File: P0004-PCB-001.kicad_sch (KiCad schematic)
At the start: 24 parts, among them CN1 Molex 105057-0001, CN2 104031-0811, CN3 Liansheng PH--00603, SW1 Khon TSB06331-090D332DA-R0500, SW2 Khon TSB06331-090D332DA-R0500, SW3 Khon TSB06331-090D332DA-R0500, SW4 Khon TSB06331-090D332DA-R0500

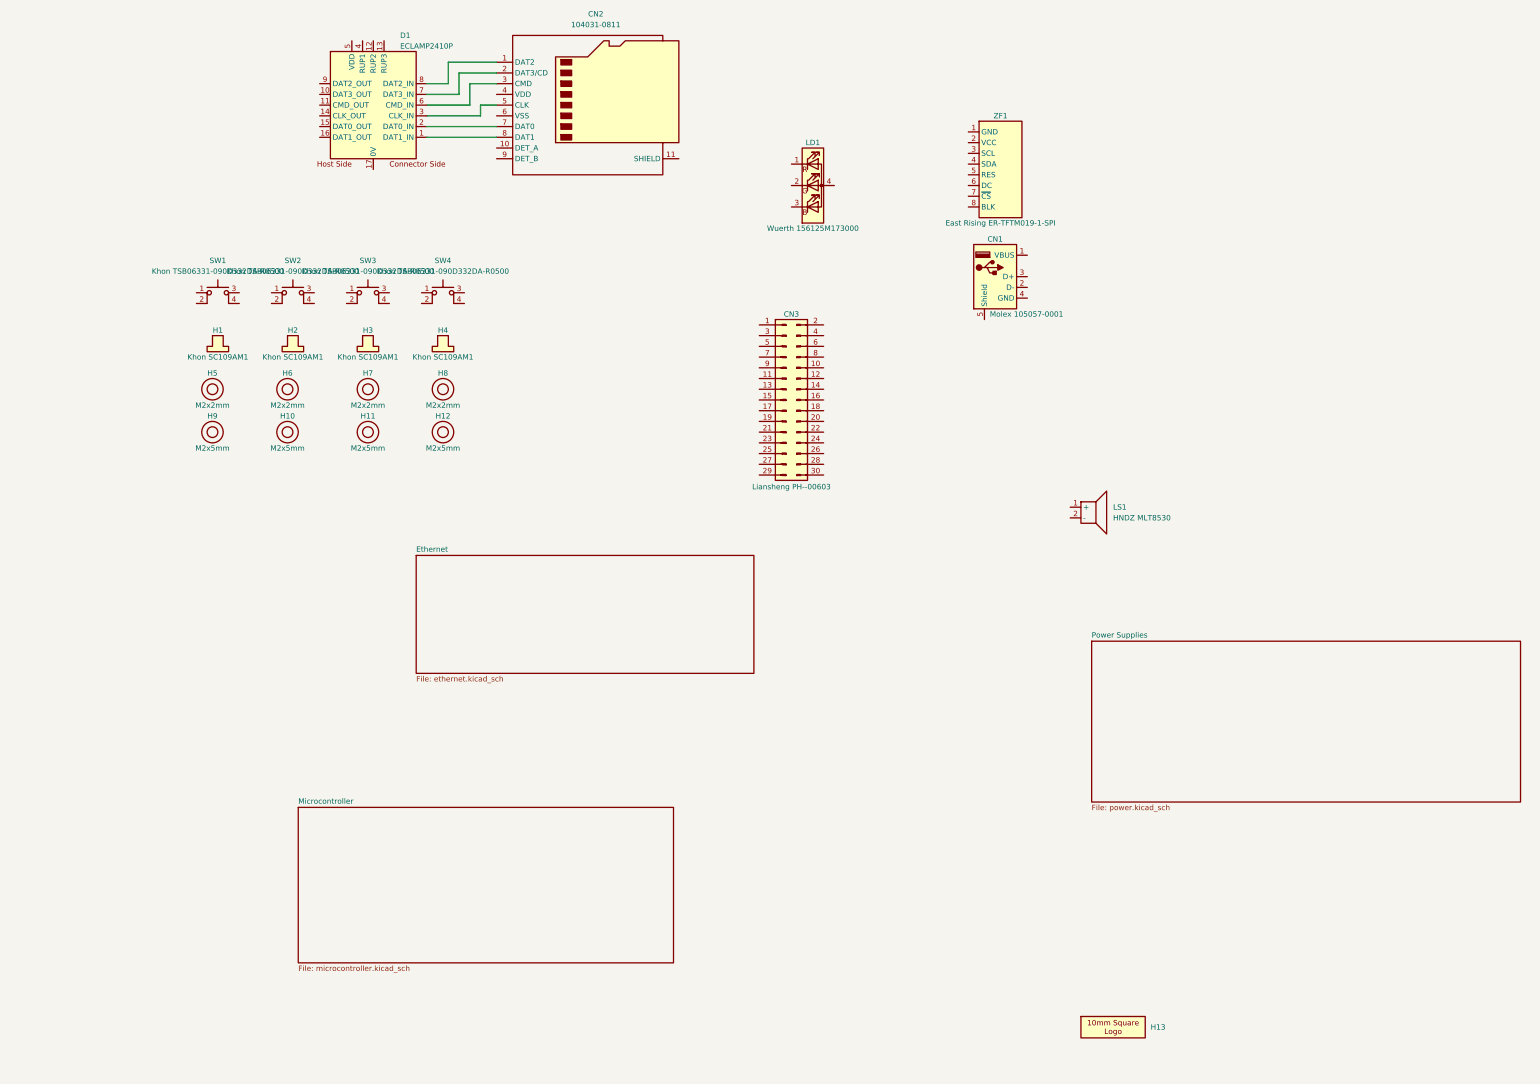
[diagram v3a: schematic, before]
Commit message: added ethernet phy
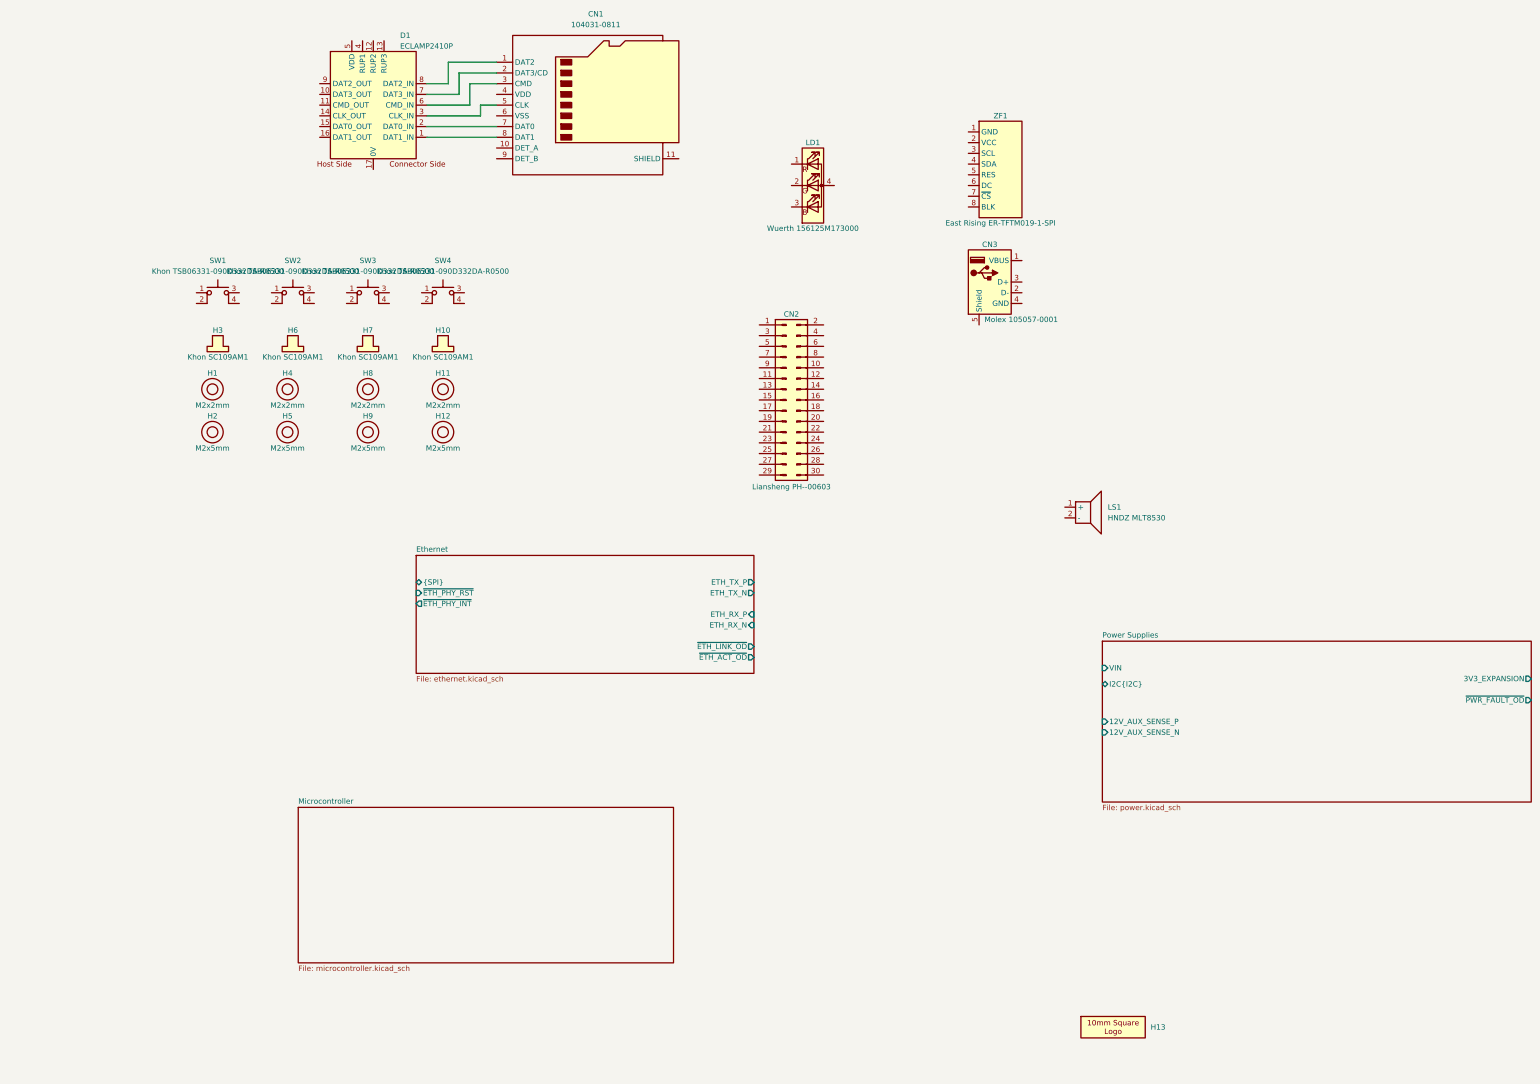
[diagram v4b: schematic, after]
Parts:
- renumbered CN2 to CN1, CN3 to CN2, CN1 to CN3, H5 to H1, H4 to H10, H8 to H11, H9 to H2, H1 to H3, H6 to H4, H10 to H5, H2 to H6, H3 to H7, H7 to H8, H11 to H9
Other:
- sheet Ethernet ports: added ETH_RX_N, ETH_RX_P, ETH_TX_N, ETH_TX_P, {SPI}, ~{ETH_ACT_OD}, ~{ETH_LINK_OD}, ~{ETH_PHY_INT}, ~{ETH_PHY_RST}; removed none
- sheet Power Supplies ports: added 12V_AUX_SENSE_N, 12V_AUX_SENSE_P, 3V3_EXPANSION, I2C{I2C}, VIN, ~{PWR_FAULT_OD}; removed none
- moved on the sheet: CN3, LS1

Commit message: layout progress
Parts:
- added D12: USBLC6-2P6, Package_TO_SOT_SMD:SOT-666, symbol Diode_WUT:ST_USBLC6-2P6
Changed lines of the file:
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@@
+	)
+	(symbol
+		(lib_id "Diode_WUT:ST_USBLC6-2P6")
+		(at 248.92 119.38 0)
+		(unit 1)
+		(body_style 1)
+		(exclude_from_sim no)
+		(in_bom yes)
+		(on_board yes)
+		(in_pos_files yes)
+		(dnp no)
+		(fields_autoplaced yes)
+		(property "Reference" "D12"
+			(at 250.19 115.57 0)
+			(show_name no)
+			(do_not_autoplace yes)
+			(effects
+				(font
+					(size 1.27 1.27)
+				)
+				(justify left)
+			)
+		)
+		(property "Value" "USBLC6-2P6"
+			(at 250.19 126.365 0)
+			(show_name no)
+			(do_not_autoplace yes)
+			(effects
+				(font
+					(size 1.27 1.27)
+				)
+				(justify left)
+			)
+		)
+		(property "Footprint" "Package_TO_SOT_SMD:SOT-666"
+			(at 248.92 119.38 0)
+			(hide yes)
+			(show_name no)
+			(do_not_autoplace no)
+			(effects
+				(font
+					(size 1.27 1.27)
+				)
+			)
+		)
+		(property "Datasheet" "https://www.st.com/content/ccc/resource/technical/document/datasheet/06/1d/48/9c/6c/20/4a/b2/CD00050750.pdf/files/CD00050750.pdf/jcr:content/translations/en.CD00050750.pdf"
+			(at 248.92 119.38 0)
+			(hide yes)
+			(show_name no)
+			(do_not_autoplace no)
+			(effects
+				(font
+					(size 1.27 1.27)
+				)
+			)
+		)
+		(property "Description" ""
+			(at 248.92 119.38 0)
+			(hide yes)
+			(show_name no)
+			(do_not_autoplace no)
+			(effects
+				(font
+					(size 1.27 1.27)
+				)
+			)
+		)
+		(property "Manufacturer" "ST"
+			(at 248.92 119.38 0)
+			(hide yes)
+			(show_name no)
+			(do_not_autoplace no)
+			(effects
+				(font
+					(size 1.27 1.27)
+				)
+			)
+		)
+		(property "MPN" "USBLC6-2P6"
+			(at 248.92 119.38 0)
+			(hide yes)
+			(show_name no)
+			(do_not_autoplace no)
+			(effects
+				(font
+					(size 1.27 1.27)
+				)
+			)
+		)
+		(pin "6"
+		)
+		(pin "4"
+		)
+		(pin "3"
+		)
+		(pin "2"
+		)
+		(pin "5"
+		)
+		(pin "1"
+		)
+		(instances
+			(project "P0004-PCB-001"
+				(path "/acdb93e6-9aa6-4a78-8a68-9d0ae3318f45"
+					(reference "D12")
+					(unit 1)
+				)
+			)
+		)
 	)
 	(symbol

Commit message: wup
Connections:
- net at D12.1 (I/O1): now also CN3.3 (D+)
- net at D12.3 (I/O2): now also CN3.2 (D-)
- net 5V_VBUS: now reaches CN3.1 (VBUS)
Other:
- moved on the sheet: D12
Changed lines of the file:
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@@
+	(wire
+		(pts
+			(xy 251.46 93.98) (xy 259.08 93.98)
+		)
+		(stroke
+			(width 0)
+			(type default)
+		)
+	)
+	(wire
+		(pts
+			(xy 251.46 96.52) (xy 259.08 96.52)
+		)
+		(stroke
+			(width 0)
+			(type default)
+		)
+	)
 	(wire
 		(pts
@@
 	(wire
 		(pts
-			(xy 110.49 54.61) (xy 123.19 54.61)
+			(xy 256.54 86.36) (xy 256.54 88.9)
 		)
 		(stroke
@@
 	(wire
 		(pts
-			(xy 115.57 46.99) (xy 110.49 46.99)
+			(xy 110.49 54.61) (xy 123.19 54.61)
 		)
 		(stroke
@@
 	(wire
 		(pts
-			(xy 115.57 41.91) (xy 115.57 46.99)
+			(xy 115.57 46.99) (xy 110.49 46.99)
 		)
 		(stroke
@@
 	(wire
 		(pts
-			(xy 123.19 52.07) (xy 127 52.07)
+			(xy 115.57 41.91) (xy 115.57 46.99)
 		)
 		(stroke
@@
 	(wire
 		(pts
-			(xy 120.65 52.07) (xy 120.65 46.99)
+			(xy 123.19 52.07) (xy 127 52.07)
 		)
 		(stroke
@@
 	(wire
 		(pts
-			(xy 110.49 59.69) (xy 127 59.69)
+			(xy 120.65 52.07) (xy 120.65 46.99)
 		)
 		(stroke
@@
 	(wire
 		(pts
-			(xy 110.49 49.53) (xy 118.11 49.53)
+			(xy 110.49 59.69) (xy 127 59.69)
 		)
 		(stroke
@@
 	(wire
 		(pts
-			(xy 118.11 44.45) (xy 127 44.45)
+			(xy 110.49 49.53) (xy 118.11 49.53)
 		)
 		(stroke
@@
 	(wire
 		(pts
-			(xy 110.49 57.15) (xy 127 57.15)
+			(xy 118.11 44.45) (xy 127 44.45)
 		)
 		(stroke
@@
 	(wire
 		(pts
-			(xy 120.65 46.99) (xy 127 46.99)
+			(xy 110.49 57.15) (xy 127 57.15)
 		)
 		(stroke
@@
 	(wire
 		(pts
-			(xy 118.11 49.53) (xy 118.11 44.45)
+			(xy 120.65 46.99) (xy 127 46.99)
 		)
 		(stroke
@@
 	(wire
 		(pts
-			(xy 110.49 52.07) (xy 120.65 52.07)
+			(xy 118.11 49.53) (xy 118.11 44.45)
 		)
 		(stroke
@@
 	(wire
 		(pts
+			(xy 110.49 52.07) (xy 120.65 52.07)
+		)
+		(stroke
+			(width 0)
+			(type default)
+		)
+	)
+	(wire
+		(pts
 			(xy 127 41.91) (xy 115.57 41.91)
+		)
+		(stroke
+			(width 0)
+			(type default)
+		)
+	)
+	(wire
+		(pts
+			(xy 256.54 88.9) (xy 251.46 88.9)
 		)
 		(stroke
@@
 	(symbol
 		(lib_id "Diode_WUT:ST_USBLC6-2P6")
-		(at 248.92 119.38 0)
+		(at 264.16 93.98 0)
 		(unit 1)
 		(body_style 1)
@@
 		(fields_autoplaced yes)
 		(property "Reference" "D12"
-			(at 250.19 115.57 0)
+			(at 265.43 90.17 0)
 			(show_name no)
 			(do_not_autoplace yes)
@@
 		)
 		(property "Value" "USBLC6-2P6"
-			(at 250.19 126.365 0)
+			(at 265.43 100.965 0)
 			(show_name no)
 			(do_not_autoplace yes)
@@
 		)
 		(property "Footprint" "Package_TO_SOT_SMD:SOT-666"
-			(at 248.92 119.38 0)
+			(at 264.16 93.98 0)
 			(hide yes)
 			(show_name no)
@@
 		)
 		(property "Datasheet" "https://www.st.com/content/ccc/resource/technical/document/datasheet/06/1d/48/9c/6c/20/4a/b2/CD00050750.pdf/files/CD00050750.pdf/jcr:content/translations/en.CD00050750.pdf"
-			(at 248.92 119.38 0)
+			(at 264.16 93.98 0)
 			(hide yes)
 			(show_name no)
@@
 		)
 		(property "Description" ""
-			(at 248.92 119.38 0)
+			(at 264.16 93.98 0)
 			(hide yes)
 			(show_name no)
@@
 		)
 		(property "Manufacturer" "ST"
-			(at 248.92 119.38 0)
+			(at 264.16 93.98 0)
 			(hide yes)
 			(show_name no)
@@
 		)
 		(property "MPN" "USBLC6-2P6"
-			(at 248.92 119.38 0)
+			(at 264.16 93.98 0)
 			(hide yes)
 			(show_name no)
@@
 					(unit 1)
 				)
+			)
+		)
+	)
+	(symbol
+		(lib_id "Power_WUT:3V3")
+		(at 256.54 86.36 0)
+		(unit 1)
+		(body_style 1)
+		(exclude_from_sim no)
+		(in_bom no)
+		(on_board no)
+		(in_pos_files yes)
+		(dnp no)
+		(fields_autoplaced yes)
+		(property "Reference" "#PWR028"
+			(at 255.905 89.535 0)
+			(hide yes)
+			(show_name no)
+			(do_not_autoplace no)
+			(effects
+				(font
+					(size 1.27 1.27)
+				)
+			)
+		)
+		(property "Value" "5V_VBUS"
+			(at 256.54 82.55 0)
+			(show_name no)
+			(do_not_autoplace yes)
+			(effects
+				(font
+					(size 1.27 1.27)
+				)
+			)
+		)
+		(property "Footprint" ""
+			(at 256.54 86.36 0)
+			(hide yes)
+			(show_name no)
+			(do_not_autoplace no)
+			(effects
+				(font
+					(size 1.27 1.27)
+				)
+			)
+		)
+		(property "Datasheet" ""
+			(at 256.54 86.36 0)
+			(hide yes)
+			(show_name no)
+			(do_not_autoplace no)
+			(effects
+				(font
+					(size 1.27 1.27)
+				)
+			)
+		)
+		(property "Description" ""
+			(at 256.54 86.36 0)
+			(hide yes)
+			(show_name no)
+			(do_not_autoplace no)
+			(effects
+				(font
+					(size 1.27 1.27)
+				)
+			)
+		)
+		(pin "1"
+		)
+		(instances
+			(project "P0004-PCB-001"
+				(path "/acdb93e6-9aa6-4a78-8a68-9d0ae3318f45"
+					(reference "#PWR028")
+					(unit 1)
+				)

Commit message: did a few little bits on layout
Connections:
- net 5V_VBUS: now also D12.5 (VBUS)
- net 0V: now reaches D12.2 (GND)
- net 0V: now also CN3.4 (GND)
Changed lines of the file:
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@@
 	(generator_version "10.0")
 	(paper "A3")
+	(junction
+		(at 264.16 104.14)
+		(diameter 0)
+		(color 0 0 0 0)
+	)
+	(junction
+		(at 264.16 86.36)
+		(diameter 0)
+		(color 0 0 0 0)
+	)
+	(wire
+		(pts
+			(xy 251.46 88.9) (xy 256.54 88.9)
+		)
+		(stroke
+			(width 0)
+			(type default)
+		)
+	)
+	(wire
+		(pts
+			(xy 251.46 99.06) (xy 256.54 99.06)
+		)
+		(stroke
+			(width 0)
+			(type default)
+		)
+	)
 	(wire
 		(pts
@@
 	(wire
 		(pts
-			(xy 256.54 86.36) (xy 256.54 88.9)
+			(xy 264.16 104.14) (xy 264.16 106.68)
 		)
 		(stroke
@@
 	(wire
 		(pts
-			(xy 110.49 54.61) (xy 123.19 54.61)
+			(xy 264.16 83.82) (xy 264.16 86.36)
 		)
 		(stroke
@@
 	(wire
 		(pts
-			(xy 115.57 46.99) (xy 110.49 46.99)
+			(xy 110.49 54.61) (xy 123.19 54.61)
 		)
 		(stroke
@@
 	(wire
 		(pts
-			(xy 115.57 41.91) (xy 115.57 46.99)
+			(xy 115.57 46.99) (xy 110.49 46.99)
 		)
 		(stroke
@@
 	(wire
 		(pts
-			(xy 123.19 52.07) (xy 127 52.07)
+			(xy 115.57 41.91) (xy 115.57 46.99)
 		)
 		(stroke
@@
 	(wire
 		(pts
-			(xy 120.65 52.07) (xy 120.65 46.99)
+			(xy 123.19 52.07) (xy 127 52.07)
 		)
 		(stroke
@@
 	(wire
 		(pts
-			(xy 110.49 59.69) (xy 127 59.69)
+			(xy 256.54 86.36) (xy 264.16 86.36)
 		)
 		(stroke
@@
 	(wire
 		(pts
-			(xy 110.49 49.53) (xy 118.11 49.53)
+			(xy 256.54 104.14) (xy 264.16 104.14)
 		)
 		(stroke
@@
 	(wire
 		(pts
-			(xy 118.11 44.45) (xy 127 44.45)
+			(xy 120.65 52.07) (xy 120.65 46.99)
 		)
 		(stroke
@@
 	(wire
 		(pts
-			(xy 110.49 57.15) (xy 127 57.15)
+			(xy 264.16 86.36) (xy 264.16 88.9)
 		)
 		(stroke
@@
 	(wire
 		(pts
-			(xy 120.65 46.99) (xy 127 46.99)
+			(xy 110.49 59.69) (xy 127 59.69)
 		)
 		(stroke
@@
 	(wire
 		(pts
-			(xy 118.11 49.53) (xy 118.11 44.45)
+			(xy 110.49 49.53) (xy 118.11 49.53)
 		)
 		(stroke
@@
 	(wire
 		(pts
-			(xy 110.49 52.07) (xy 120.65 52.07)
+			(xy 118.11 44.45) (xy 127 44.45)
 		)
 		(stroke
@@
 	(wire
 		(pts
-			(xy 127 41.91) (xy 115.57 41.91)
+			(xy 256.54 99.06) (xy 256.54 104.14)
 		)
 		(stroke
@@
 	(wire
 		(pts
-			(xy 256.54 88.9) (xy 251.46 88.9)
+			(xy 110.49 57.15) (xy 127 57.15)
+		)
+		(stroke
+			(width 0)
+			(type default)
+		)
+	)
+	(wire
+		(pts
+			(xy 120.65 46.99) (xy 127 46.99)
+		)
+		(stroke
+			(width 0)
+			(type default)
+		)
+	)
+	(wire
+		(pts
+			(xy 256.54 88.9) (xy 256.54 86.36)
+		)
+		(stroke
+			(width 0)
+			(type default)
+		)
+	)
+	(wire
+		(pts
+			(xy 118.11 49.53) (xy 118.11 44.45)
+		)
+		(stroke
+			(width 0)
+			(type default)
+		)
+	)
+	(wire
+		(pts
+			(xy 110.49 52.07) (xy 120.65 52.07)
+		)
+		(stroke
+			(width 0)
+			(type default)
+		)
+	)
+	(wire
+		(pts
+			(xy 264.16 101.6) (xy 264.16 104.14)
+		)
+		(stroke
+			(width 0)
+			(type default)
+		)
+	)
+	(wire
+		(pts
+			(xy 127 41.91) (xy 115.57 41.91)
 		)
 		(stroke
@@
 	(symbol
 		(lib_id "Power_WUT:3V3")
-		(at 256.54 86.36 0)
+		(at 264.16 83.82 0)
 		(unit 1)
 		(body_style 1)
@@
 		(fields_autoplaced yes)
 		(property "Reference" "#PWR028"
-			(at 255.905 89.535 0)
+			(at 263.525 86.995 0)
 			(hide yes)
 			(show_name no)
@@
 		)
 		(property "Value" "5V_VBUS"
-			(at 256.54 82.55 0)
+			(at 264.16 80.01 0)
 			(show_name no)
 			(do_not_autoplace yes)
@@
 		)
 		(property "Footprint" ""
-			(at 256.54 86.36 0)
+			(at 264.16 83.82 0)
 			(hide yes)
 			(show_name no)
@@
 		)
 		(property "Datasheet" ""
-			(at 256.54 86.36 0)
+			(at 264.16 83.82 0)
 			(hide yes)
 			(show_name no)
@@
 		)
 		(property "Description" ""
-			(at 256.54 86.36 0)
+			(at 264.16 83.82 0)
 			(hide yes)
 			(show_name no)
@@
 					(unit 1)
 				)
+			)
+		)
+	)
+	(symbol
+		(lib_id "Power_WUT:0V")
+		(at 264.16 106.68 0)
+		(unit 1)
+		(body_style 1)
+		(exclude_from_sim no)
+		(in_bom no)
+		(on_board no)
+		(in_pos_files yes)
+		(dnp no)
+		(fields_autoplaced yes)
+		(property "Reference" "#PWR031"
+			(at 264.16 106.68 0)
+			(hide yes)
+			(show_name no)
+			(do_not_autoplace no)
+			(effects
+				(font
+					(size 1.27 1.27)
+				)
+			)
+		)
+		(property "Value" "0V"
+			(at 264.16 110.49 0)
+			(show_name no)
+			(do_not_autoplace yes)
+			(effects
+				(font
+					(size 1.27 1.27)
+				)
+			)
+		)
+		(property "Footprint" ""
+			(at 264.16 106.68 0)
+			(hide yes)
+			(show_name no)
+			(do_not_autoplace no)
+			(effects
+				(font
+					(size 1.27 1.27)
+				)
+			)
+		)
+		(property "Datasheet" ""
+			(at 264.16 106.68 0)
+			(hide yes)
+			(show_name no)
+			(do_not_autoplace no)
+			(effects
+				(font
+					(size 1.27 1.27)
+				)
+			)
+		)
+		(property "Description" ""
+			(at 264.16 106.68 0)
+			(hide yes)
+			(show_name no)
+			(do_not_autoplace no)
+			(effects
+				(font
+					(size 1.27 1.27)
+				)
+			)
+		)
+		(pin "1"
+		)
+		(instances
+			(project "P0004-PCB-001"
+				(path "/acdb93e6-9aa6-4a78-8a68-9d0ae3318f45"
+					(reference "#PWR031")
+					(unit 1)
+				)

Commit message: more progress
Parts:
- removed CN1: 104031-0811, Connector_WUT:microSD_HC_Molex_104031-0811, symbol Connector_WUT:Molex_104031-0811
- removed CN3: Molex 105057-0001, Connector_WUT:USB-A_Molex_105057-0001_TH_Vertical, symbol Connector_WUT:Molex_105057-0001
- removed D1: ECLAMP2410P, Diode_WUT:Semtech_ECLAMP2410P, symbol Diode_WUT:Semtech_EClamp2410P
- removed D12: USBLC6-2P6, Package_TO_SOT_SMD:SOT-666, symbol Diode_WUT:ST_USBLC6-2P6
- removed LD1: Wuerth 156125M173000, LED_WUT:Wuerth_156125M173000, symbol LED_WUT:Wuerth_156125M173000
- removed ZF1: East Rising ER-TFTM019-1-SPI, Display_WUT:East-Rising_ER-TFTM019-1-SPI, symbol Display_WUT:East-Rising_ER-TFTM019-1-SPI
- renumbered CN2 to CN1
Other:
- sheet Microcontroller ports: added USB_VBUS_EN, {SPI}, ~{ETH_PHY_INT}, ~{ETH_PHY_RESET}, ~{USB_VBUS_FAULT}; removed none
- sheet Power Supplies ports: added VBUS_EN, ~{VBUS_FAULT}; removed 12V_AUX_SENSE_N, 12V_AUX_SENSE_P, 3V3_EXPANSION, I2C{I2C}, ~{PWR_FAULT_OD}
